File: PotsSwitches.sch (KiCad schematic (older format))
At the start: 17 parts

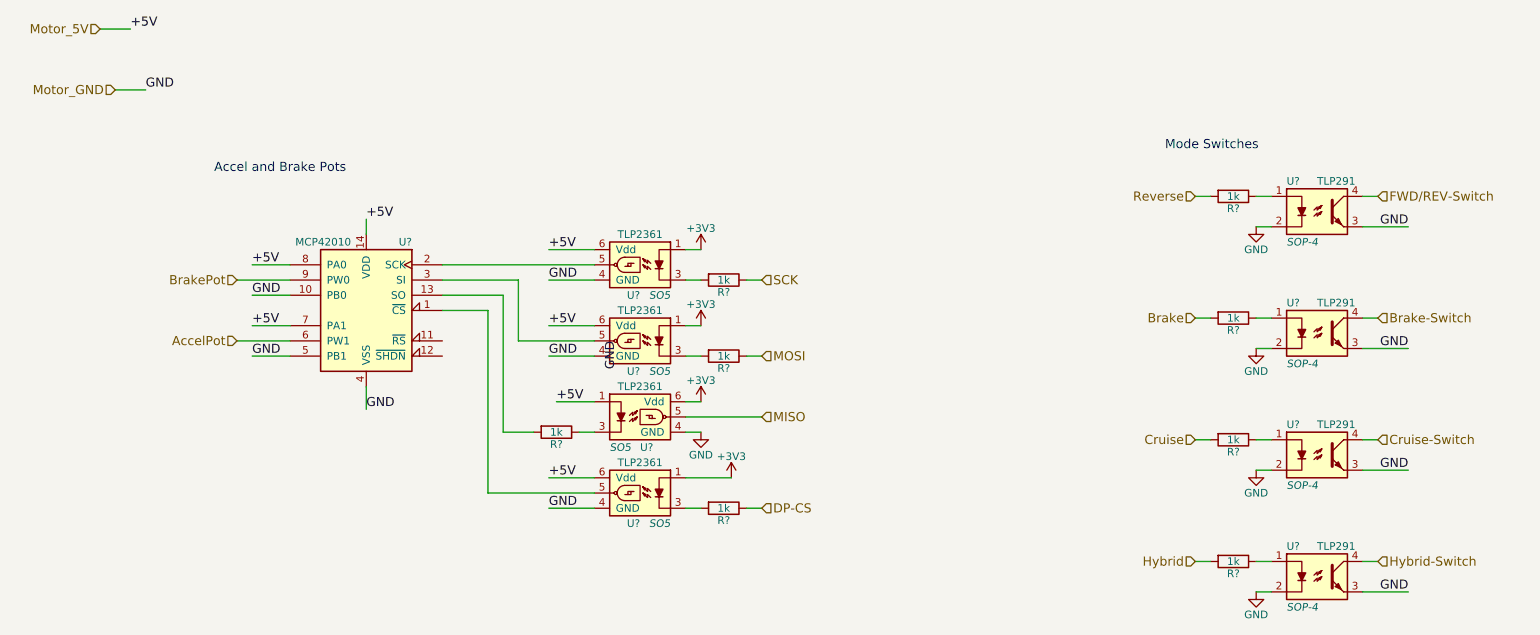
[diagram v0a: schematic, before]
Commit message: most associations, started pcb
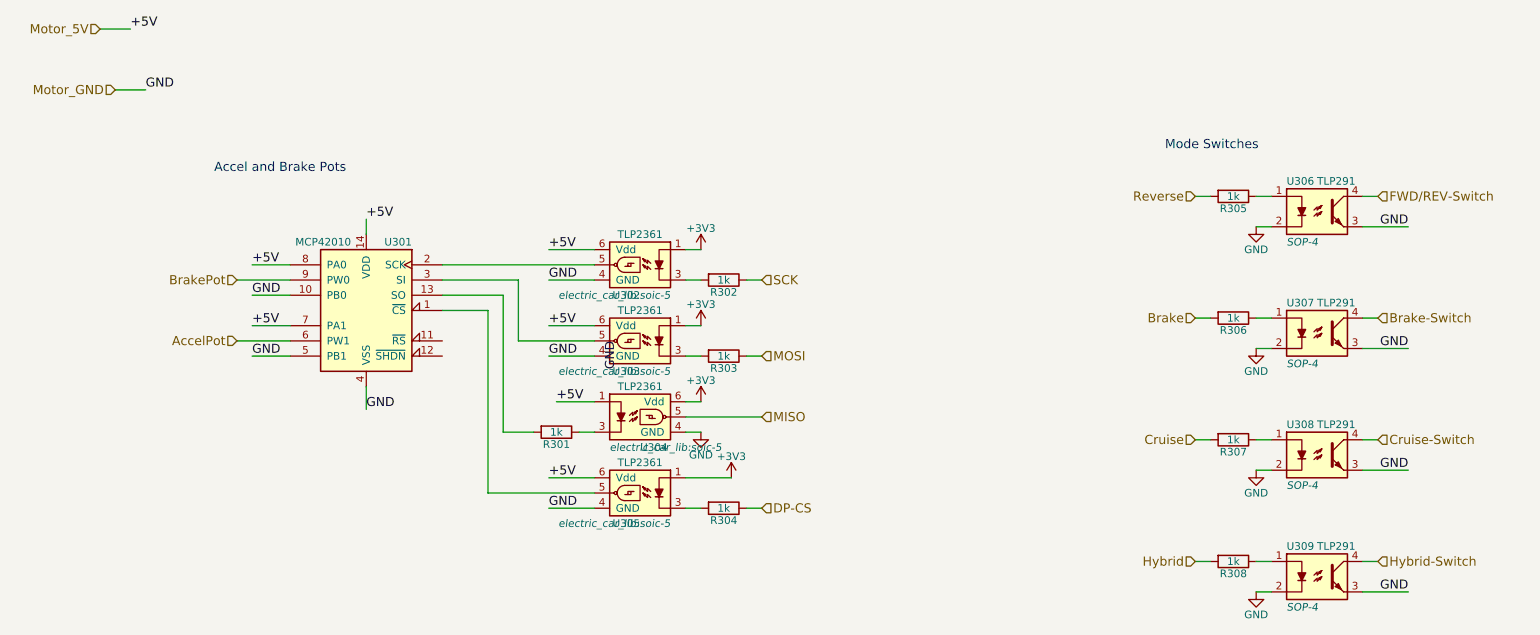
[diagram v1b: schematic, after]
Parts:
- R301, R302, R303, R304, R305, R306, R307, R308: renamed from R?; footprint (none) -> Resistors_SMD:R_1206_HandSoldering
- U302, U303, U304, U305: renamed from U?; footprint SO5 -> electric_car_lib:soic-5
- gave numbers to parts that had none: 5
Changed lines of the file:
@@
 $EndDescr
 $Comp
-L MCP42010 U?
+L MCP42010 U301
 U 1 1 582ABDBA
 P 2750 2550
-F 0 "U?" H 2450 3000 50  0000 L CNN
+F 0 "U301" H 2450 3000 50  0000 L CNN
 F 1 "MCP42010" H 2850 3000 50  0000 L CNN
 F 2 "Housings_SOIC:SOIC-14_3.9x8.7mm_Pitch1.27mm" H 2750 2650 50  0001 C CNN
@@
 Accel and Brake Pots
 $Comp
-L GND #PWR?
+L GND #PWR044
 U 1 1 582ABDC8
 P 8600 3600
-F 0 "#PWR?" H 8600 3350 50  0001 C CNN
+F 0 "#PWR044" H 8600 3350 50  0001 C CNN
 F 1 "GND" H 8600 3450 50  0000 C CNN
 F 2 "" H 8600 3600 50  0000 C CNN
@@
 	9400 1800 9300 1800
 $Comp
-L R R?
+L R R305
 U 1 1 582ABDC9
 P 8450 1800
-F 0 "R?" V 8530 1800 50  0000 C CNN
+F 0 "R305" V 8530 1800 50  0000 C CNN
 F 1 "1k" V 8450 1800 50  0000 C CNN
-F 2 "" V 8380 1800 50  0000 C CNN
+F 2 "Resistors_SMD:R_1206_HandSoldering" V 8380 1800 50  0001 C CNN
 F 3 "" H 8450 1800 50  0000 C CNN
 	1    8450 1800
@@
 	9400 2600 9300 2600
 $Comp
-L R R?
+L R R306
 U 1 1 582ABDD2
 P 8450 2600
-F 0 "R?" V 8530 2600 50  0000 C CNN
+F 0 "R306" V 8530 2600 50  0000 C CNN
 F 1 "1k" V 8450 2600 50  0000 C CNN
-F 2 "" V 8380 2600 50  0000 C CNN
+F 2 "Resistors_SMD:R_1206_HandSoldering" V 8380 2600 50  0001 C CNN
 F 3 "" H 8450 2600 50  0000 C CNN
 	1    8450 2600
@@
 	9400 3400 9300 3400
 $Comp
-L R R?
+L R R307
 U 1 1 582ABDD6
 P 8450 3400
-F 0 "R?" V 8530 3400 50  0000 C CNN
+F 0 "R307" V 8530 3400 50  0000 C CNN
 F 1 "1k" V 8450 3400 50  0000 C CNN
-F 2 "" V 8380 3400 50  0000 C CNN
+F 2 "Resistors_SMD:R_1206_HandSoldering" V 8380 3400 50  0001 C CNN
 F 3 "" H 8450 3400 50  0000 C CNN
 	1    8450 3400
@@
 	9400 4200 9300 4200
 $Comp
-L R R?
+L R R308
 U 1 1 582ABDDA
 P 8450 4200
-F 0 "R?" V 8530 4200 50  0000 C CNN
+F 0 "R308" V 8530 4200 50  0000 C CNN
 F 1 "1k" V 8450 4200 50  0000 C CNN
-F 2 "" V 8380 4200 50  0000 C CNN
+F 2 "Resistors_SMD:R_1206_HandSoldering" V 8380 4200 50  0001 C CNN
 F 3 "" H 8450 4200 50  0000 C CNN
 	1    8450 4200
@@
 $EndComp
 $Comp
-L TLP2361 U?
+L TLP2361 U304
 U 1 1 582ABDEC
 P 4550 3250
-F 0 "U?" H 4550 3050 50  0000 L CNN
+F 0 "U304" H 4550 3050 50  0000 L CNN
 F 1 "TLP2361" H 4550 3450 50  0000 C CNN
-F 2 "SO5" H 4350 3050 50  0000 L CIN
+F 2 "electric_car_lib:soic-5" H 4350 3050 50  0000 L CIN
 F 3 "" H 4550 3250 50  0000 L CNN
 	1    4550 3250
@@
 $EndComp
 $Comp
-L TLP2361 U?
+L TLP2361 U305
 U 1 1 582ABDED
 P 4550 3750
-F 0 "U?" H 4550 3550 50  0000 L CNN
+F 0 "U305" H 4550 3550 50  0000 L CNN
 F 1 "TLP2361" H 4550 3950 50  0000 C CNN
-F 2 "SO5" H 4350 3550 50  0000 L CIN
+F 2 "electric_car_lib:soic-5" H 4350 3550 50  0000 L CIN
 F 3 "" H 4550 3750 50  0000 L CNN
 	1    4550 3750
@@
 $EndComp
 $Comp
-L TLP2361 U?
+L TLP2361 U303
 U 1 1 582ABDEE
 P 4550 2750
-F 0 "U?" H 4550 2550 50  0000 L CNN
+F 0 "U303" H 4550 2550 50  0000 L CNN
 F 1 "TLP2361" H 4550 2950 50  0000 C CNN
-F 2 "SO5" H 4350 2550 50  0000 L CIN
+F 2 "electric_car_lib:soic-5" H 4350 2550 50  0000 L CIN
 F 3 "" H 4550 2750 50  0000 L CNN
 	1    4550 2750
@@
 $EndComp
 $Comp
-L TLP2361 U?
+L TLP2361 U302
 U 1 1 582ABDEF
 P 4550 2250
-F 0 "U?" H 4550 2050 50  0000 L CNN
+F 0 "U302" H 4550 2050 50  0000 L CNN
 F 1 "TLP2361" H 4550 2450 50  0000 C CNN
-F 2 "SO5" H 4350 2050 50  0000 L CIN
+F 2 "electric_car_lib:soic-5" H 4350 2050 50  0000 L CIN
 F 3 "" H 4550 2250 50  0000 L CNN
 	1    4550 2250
@@
 $EndComp
 $Comp
-L GND #PWR?
+L GND #PWR045
 U 1 1 582ABDF1
 P 4950 3350
-F 0 "#PWR?" H 4950 3100 50  0001 C CNN
+F 0 "#PWR045" H 4950 3100 50  0001 C CNN
 F 1 "GND" H 4950 3200 50  0000 C CNN
 F 2 "" H 4950 3350 50  0000 C CNN
@@
 GND
 $Comp
-L R R?
+L R R302
 U 1 1 582ABDF2
 P 5100 2350
-F 0 "R?" V 5180 2350 50  0000 C CNN
+F 0 "R302" V 5180 2350 50  0000 C CNN
 F 1 "1k" V 5100 2350 50  0000 C CNN
-F 2 "" V 5030 2350 50  0000 C CNN
+F 2 "Resistors_SMD:R_1206_HandSoldering" V 5030 2350 50  0001 C CNN
 F 3 "" H 5100 2350 50  0000 C CNN
 	1    5100 2350
@@
 $EndComp
 $Comp
-L R R?
+L R R303
 U 1 1 582AD716
 P 5100 2850
-F 0 "R?" V 5180 2850 50  0000 C CNN
+F 0 "R303" V 5180 2850 50  0000 C CNN
 F 1 "1k" V 5100 2850 50  0000 C CNN
-F 2 "" V 5030 2850 50  0000 C CNN
+F 2 "Resistors_SMD:R_1206_HandSoldering" V 5030 2850 50  0001 C CNN
 F 3 "" H 5100 2850 50  0000 C CNN
 	1    5100 2850
@@
 $EndComp
 $Comp
-L R R?
+L R R304
 U 1 1 582AD7A9
 P 5100 3850
-F 0 "R?" V 5180 3850 50  0000 C CNN
+F 0 "R304" V 5180 3850 50  0000 C CNN
 F 1 "1k" V 5100 3850 50  0000 C CNN
-F 2 "" V 5030 3850 50  0000 C CNN
+F 2 "Resistors_SMD:R_1206_HandSoldering" V 5030 3850 50  0001 C CNN
 F 3 "" H 5100 3850 50  0000 C CNN
 	1    5100 3850
@@
 $EndComp
 $Comp
-L R R?
+L R R301
 U 1 1 582AD82B
 P 4000 3350
-F 0 "R?" V 4080 3350 50  0000 C CNN
+F 0 "R301" V 4080 3350 50  0000 C CNN
 F 1 "1k" V 4000 3350 50  0000 C CNN
-F 2 "" V 3930 3350 50  0000 C CNN
+F 2 "Resistors_SMD:R_1206_HandSoldering" V 3930 3350 50  0001 C CNN
 F 3 "" H 4000 3350 50  0000 C CNN
 	1    4000 3350
@@
 	5350 2350 5250 2350
 $Comp
-L +3V3 #PWR?
+L +3V3 #PWR046
 U 1 1 582AE728
 P 4950 3150
-F 0 "#PWR?" H 4950 3000 50  0001 C CNN
+F 0 "#PWR046" H 4950 3000 50  0001 C CNN
 F 1 "+3V3" H 4950 3290 50  0000 C CNN
 F 2 "" H 4950 3150 50  0000 C CNN
@@
 	4950 3850 4850 3850
 $Comp
-L +3V3 #PWR?
+L +3V3 #PWR047
 U 1 1 582AEEE5
 P 4950 2150
-F 0 "#PWR?" H 4950 2000 50  0001 C CNN
+F 0 "#PWR047" H 4950 2000 50  0001 C CNN
 F 1 "+3V3" H 4950 2290 50  0000 C CNN
 F 2 "" H 4950 2150 50  0000 C CNN
@@
 $EndComp
 $Comp
-L +3V3 #PWR?
+L +3V3 #PWR048
 U 1 1 582AEF3B
 P 4950 2650
-F 0 "#PWR?" H 4950 2500 50  0001 C CNN
+F 0 "#PWR048" H 4950 2500 50  0001 C CNN
 F 1 "+3V3" H 4950 2790 50  0000 C CNN
 F 2 "" H 4950 2650 50  0000 C CNN
@@
 $EndComp
 $Comp
-L +3V3 #PWR?
+L +3V3 #PWR049
 U 1 1 582AEF91
 P 5150 3650
-F 0 "#PWR?" H 5150 3500 50  0001 C CNN
+F 0 "#PWR049" H 5150 3500 50  0001 C CNN
 F 1 "+3V3" H 5150 3790 50  0000 C CNN
 F 2 "" H 5150 3650 50  0000 C CNN
@@
 Hybrid-Switch
 $Comp
-L TLP291 U?
+L TLP291 U306
 U 1 1 582B1201
 P 9000 1900
-F 0 "U?" H 8800 2100 50  0000 L CNN
+F 0 "U306" H 8800 2100 50  0000 L CNN
 F 1 "TLP291" H 9000 2100 50  0000 L CNN
 F 2 "SOP-4" H 8800 1700 50  0000 L CIN
@@
 $EndComp
 $Comp
-L TLP291 U?
+L TLP291 U307
 U 1 1 582B14A0
 P 9000 2700
-F 0 "U?" H 8800 2900 50  0000 L CNN
+F 0 "U307" H 8800 2900 50  0000 L CNN
 F 1 "TLP291" H 9000 2900 50  0000 L CNN
 F 2 "SOP-4" H 8800 2500 50  0000 L CIN
@@
 	8600 4200 8700 4200
 $Comp
-L TLP291 U?
+L TLP291 U308
 U 1 1 582B1845
 P 9000 3500
-F 0 "U?" H 8800 3700 50  0000 L CNN
+F 0 "U308" H 8800 3700 50  0000 L CNN
 F 1 "TLP291" H 9000 3700 50  0000 L CNN
 F 2 "SOP-4" H 8800 3300 50  0000 L CIN
@@
 $EndComp
 $Comp
-L TLP291 U?
+L TLP291 U309
 U 1 1 582B18AB
 P 9000 4300
-F 0 "U?" H 8800 4500 50  0000 L CNN
+F 0 "U309" H 8800 4500 50  0000 L CNN
 F 1 "TLP291" H 9000 4500 50  0000 L CNN
 F 2 "SOP-4" H 8800 4100 50  0000 L CIN
@@
 $EndComp
 $Comp
-L GND #PWR?
+L GND #PWR050
 U 1 1 582B1B80
 P 8600 4400
-F 0 "#PWR?" H 8600 4150 50  0001 C CNN
+F 0 "#PWR050" H 8600 4150 50  0001 C CNN
 F 1 "GND" H 8600 4250 50  0000 C CNN
 F 2 "" H 8600 4400 50  0000 C CNN
@@
 $EndComp
 $Comp
-L GND #PWR?
+L GND #PWR051
 U 1 1 582B1BBE
 P 8600 2800
-F 0 "#PWR?" H 8600 2550 50  0001 C CNN
+F 0 "#PWR051" H 8600 2550 50  0001 C CNN
 F 1 "GND" H 8600 2650 50  0000 C CNN
 F 2 "" H 8600 2800 50  0000 C CNN
@@
 	9600 4400 9300 4400
 $Comp
-L GND #PWR?
+L GND #PWR052
 U 1 1 582B1F30
 P 8600 2000
-F 0 "#PWR?" H 8600 1750 50  0001 C CNN
+F 0 "#PWR052" H 8600 1750 50  0001 C CNN
 F 1 "GND" H 8600 1850 50  0000 C CNN
 F 2 "" H 8600 2000 50  0000 C CNN

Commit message: changed optos, removed relay, needs ssr
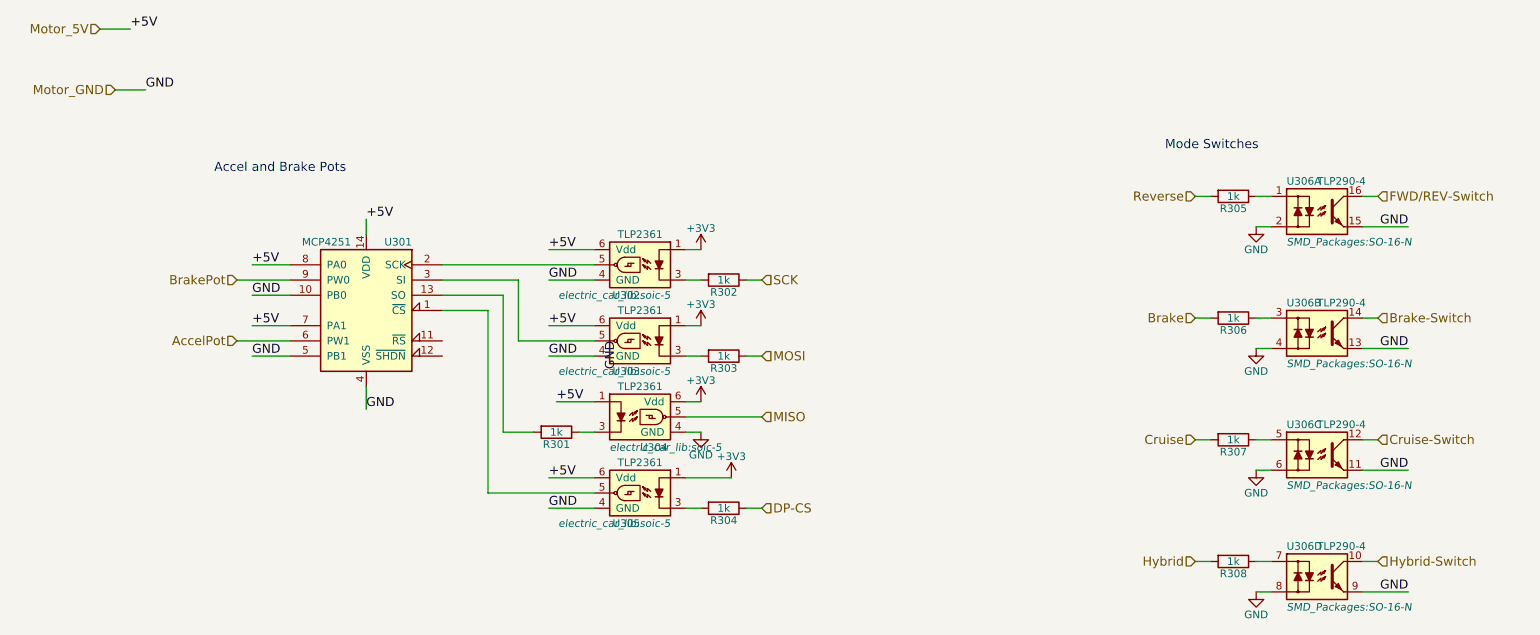
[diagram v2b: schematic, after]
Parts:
- removed U301: MCP42010, Housings_SOIC:SOIC-14_3.9x8.7mm_Pitch1.27mm, symbol MCP42010
- removed U306, U307, U308, U309: TLP291, SOP-4, symbol TLP291
- added U301: MCP4251, SMD_Packages:SOIC-14_N, symbol MCP4251
- added U306: TLP290-4, SMD_Packages:SO-16-N, symbol TLP290-4
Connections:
- net AccelPot: now also U301.6 (PW1)
- net Brake-Switch: now also U306.14
- net BrakePot: now also U301.9 (PW0)
- net Cruise-Switch: now also U306.12
- net FWD/REV-Switch: now also U306.16
- net GND: now also U301.10 (PB0), U301.4 (VSS), U301.5 (PB1), U306.11, U306.13, U306.15, U306.2, U306.4, U306.6, U306.8, U306.9
- net Hybrid-Switch: now also U306.10
- net Motor_5V: now also U301.14 (VDD), U301.7 (PA1), U301.8 (PA0)
- net at U305.5: now also U301.1 (~CS)
- net at R301.2: now also U301.13 (SO)
- net at U302.5: now also U301.2 (SCK)
- net at U303.5: now also U301.3 (SI)
- net at R305.1: now also U306.1
- net at R306.1: now also U306.3
- net at R307.1: now also U306.5
- net at R308.1: now also U306.7
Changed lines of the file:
@@
 Comment4 ""
 $EndDescr
-$Comp
-L MCP42010 U301
-U 1 1 582ABDBA
-P 2750 2550
-F 0 "U301" H 2450 3000 50  0000 L CNN
-F 1 "MCP42010" H 2850 3000 50  0000 L CNN
-F 2 "Housings_SOIC:SOIC-14_3.9x8.7mm_Pitch1.27mm" H 2750 2650 50  0001 C CNN
-F 3 "" H 2750 2650 50  0000 C CNN
-	1    2750 2550
-	-1   0    0    -1
-$EndComp
 Wire Wire Line
 	2000 2650 2250 2650
@@
 Text HLabel 9400 4200 2    60   Input ~ 0
 Hybrid-Switch
-$Comp
-L TLP291 U306
-U 1 1 582B1201
-P 9000 1900
-F 0 "U306" H 8800 2100 50  0000 L CNN
-F 1 "TLP291" H 9000 2100 50  0000 L CNN
-F 2 "SOP-4" H 8800 1700 50  0000 L CIN
-F 3 "" H 9000 1900 50  0000 L CNN
-	1    9000 1900
-	1    0    0    -1
-$EndComp
-$Comp
-L TLP291 U307
-U 1 1 582B14A0
-P 9000 2700
-F 0 "U307" H 8800 2900 50  0000 L CNN
-F 1 "TLP291" H 9000 2900 50  0000 L CNN
-F 2 "SOP-4" H 8800 2500 50  0000 L CIN
-F 3 "" H 9000 2700 50  0000 L CNN
-	1    9000 2700
-	1    0    0    -1
-$EndComp
 Wire Wire Line
 	8600 4200 8700 4200
-$Comp
-L TLP291 U308
-U 1 1 582B1845
-P 9000 3500
-F 0 "U308" H 8800 3700 50  0000 L CNN
-F 1 "TLP291" H 9000 3700 50  0000 L CNN
-F 2 "SOP-4" H 8800 3300 50  0000 L CIN
-F 3 "" H 9000 3500 50  0000 L CNN
-	1    9000 3500
-	1    0    0    -1
-$EndComp
-$Comp
-L TLP291 U309
-U 1 1 582B18AB
-P 9000 4300
-F 0 "U309" H 8800 4500 50  0000 L CNN
-F 1 "TLP291" H 9000 4500 50  0000 L CNN
-F 2 "SOP-4" H 8800 4100 50  0000 L CIN
-F 3 "" H 9000 4300 50  0000 L CNN
-	1    9000 4300
-	1    0    0    -1
-$EndComp
 $Comp
 L GND #PWR050
@@
 Text Notes 8000 1500 0    60   ~ 0
 Mode Switches
+$Comp
+L TLP290-4 U306
+U 1 1 582BD286
+P 9000 1900
+F 0 "U306" H 8800 2100 50  0000 L CNN
+F 1 "TLP290-4" H 9000 2100 50  0000 L CNN
+F 2 "SMD_Packages:SO-16-N" H 8800 1700 50  0000 L CIN
+F 3 "" H 9025 1900 50  0000 L CNN
+	1    9000 1900
+	1    0    0    -1
+$EndComp
+$Comp
+L TLP290-4 U306
+U 2 1 582BD3F7
+P 9000 2700
+F 0 "U306" H 8800 2900 50  0000 L CNN
+F 1 "TLP290-4" H 9000 2900 50  0000 L CNN
+F 2 "SMD_Packages:SO-16-N" H 8800 2500 50  0000 L CIN
+F 3 "" H 9025 2700 50  0000 L CNN
+	2    9000 2700
+	1    0    0    -1
+$EndComp
+$Comp
+L TLP290-4 U306
+U 3 1 582BD4A1
+P 9000 3500
+F 0 "U306" H 8800 3700 50  0000 L CNN
+F 1 "TLP290-4" H 9000 3700 50  0000 L CNN
+F 2 "SMD_Packages:SO-16-N" H 8800 3300 50  0000 L CIN
+F 3 "" H 9025 3500 50  0000 L CNN
+	3    9000 3500
+	1    0    0    -1
+$EndComp
+$Comp
+L TLP290-4 U306
+U 4 1 582BD513
+P 9000 4300
+F 0 "U306" H 8800 4500 50  0000 L CNN
+F 1 "TLP290-4" H 9000 4500 50  0000 L CNN
+F 2 "SMD_Packages:SO-16-N" H 8800 4100 50  0000 L CIN
+F 3 "" H 9025 4300 50  0000 L CNN
+	4    9000 4300
+	1    0    0    -1
+$EndComp
+$Comp
+L MCP4251 U301
+U 1 1 582BE8AC
+P 2750 2550
+F 0 "U301" H 2450 3000 50  0000 L CNN
+F 1 "MCP4251" H 2850 3000 50  0000 L CNN
+F 2 "SMD_Packages:SOIC-14_N" H 2750 2650 50  0001 C CNN
+F 3 "" H 2750 2650 50  0000 C CNN
+	1    2750 2550
+	-1   0    0    -1
+$EndComp
 $EndSCHEMATC
